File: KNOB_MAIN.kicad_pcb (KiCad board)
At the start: 2 copper layers, 100 x 30 mm, 25 parts, among them J1 HRO_TYPE-C-31-M-12, SW1 PEC11R-4220F-S0024, U1 LP2992AIM5X-3.3, U2 ESP32-C3-MINI-1

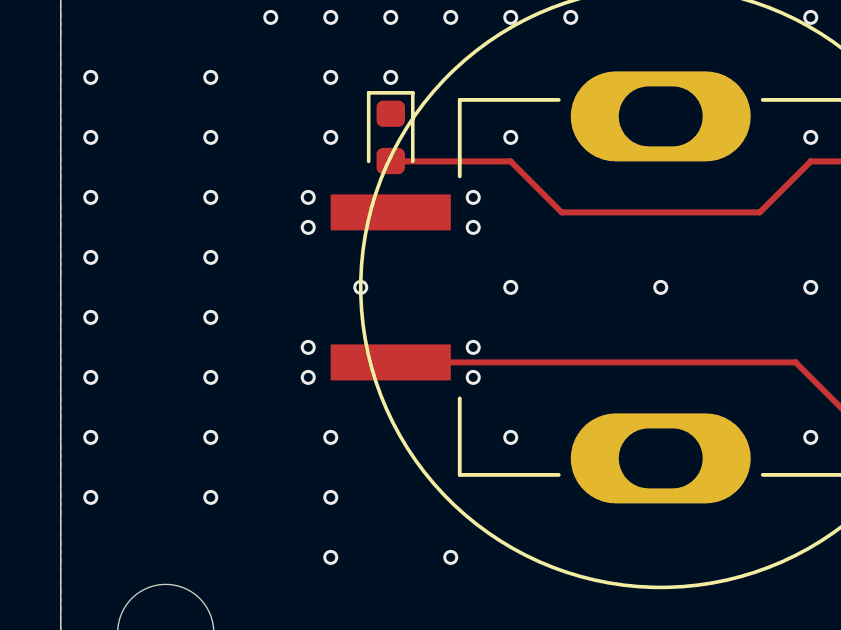
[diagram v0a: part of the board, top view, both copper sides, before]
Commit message: Add 100nF debounce capacitor to push pin
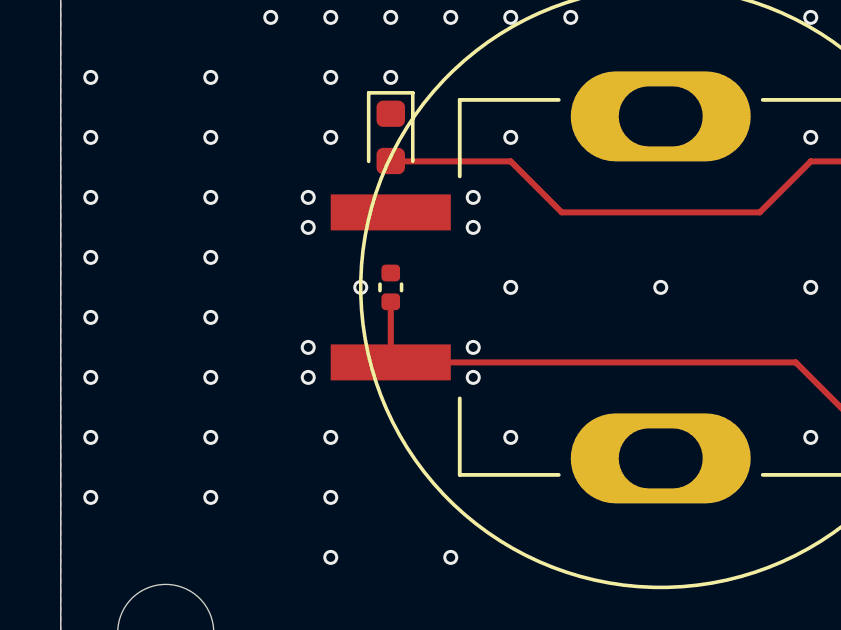
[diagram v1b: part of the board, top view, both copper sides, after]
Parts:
- added C7: 100nF, Capacitor_SMD:C_0402_1005Metric, F.Cu at (111.0, 85.0)
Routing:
- net /ENTER: track 76.2 -> 78.2 mm
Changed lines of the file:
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@@
     (thickness 1.6)
     (drawings 46)
-    (tracks 371)
+    (tracks 372)
     (zones 0)
-    (modules 25)
+    (modules 26)
     (nets 18)
   )
@@
     (diff_pair_width 0.28)
     (diff_pair_gap 0.15)
+  )
+  (module Capacitor_SMD:C_0402_1005Metric (layer F.Cu)
+    (at 111 85 90)
+    (descr "Capacitor SMD 0402 (1005 Metric), square (rectangular) end terminal, IPC_7351 nominal, (Body size source: IPC-SM-782 page 76, https://www.pcb-3d.com/wordpress/wp-content/uploads/ipc-sm-782a_amendment_1_and_2.pdf), generated with kicad-footprint-generator")
+    (tags capacitor)
+    (attr smd)
+    (fp_text reference C7 (at 0 -1.16 90) (layer F.Fab)
+      (effects (font (size 1 1) (thickness 0.15)))
+    )
+    (fp_text value 100nF (at 0 1.16 90) (layer F.Fab)
+      (effects (font (size 1 1) (thickness 0.15)))
+    )
+    (fp_line (start 0.91 0.46) (end -0.91 0.46) (layer F.CrtYd) (width 0.05))
+    (fp_line (start 0.91 -0.46) (end 0.91 0.46) (layer F.CrtYd) (width 0.05))
+    (fp_line (start -0.91 -0.46) (end 0.91 -0.46) (layer F.CrtYd) (width 0.05))
+    (fp_line (start -0.91 0.46) (end -0.91 -0.46) (layer F.CrtYd) (width 0.05))
+    (fp_line (start -0.107836 0.36) (end 0.107836 0.36) (layer F.SilkS) (width 0.12))
+    (fp_line (start -0.107836 -0.36) (end 0.107836 -0.36) (layer F.SilkS) (width 0.12))
+    (fp_line (start 0.5 0.25) (end -0.5 0.25) (layer F.Fab) (width 0.1))
+    (fp_line (start 0.5 -0.25) (end 0.5 0.25) (layer F.Fab) (width 0.1))
+    (fp_line (start -0.5 -0.25) (end 0.5 -0.25) (layer F.Fab) (width 0.1))
+    (fp_line (start -0.5 0.25) (end -0.5 -0.25) (layer F.Fab) (width 0.1))
+    (fp_text user %R (at 0 0 90) (layer F.Fab)
+      (effects (font (size 0.25 0.25) (thickness 0.04)))
+    )
+    (pad 2 smd roundrect (at 0.48 0 90) (size 0.56 0.62) (layers F.Cu F.Paste F.Mask) (roundrect_rratio 0.25)
+      (net 2 GND))
+    (pad 1 smd roundrect (at -0.48 0 90) (size 0.56 0.62) (layers F.Cu F.Paste F.Mask) (roundrect_rratio 0.25)
+      (net 9 /ENTER))
+    (model ${KISYS3DMOD}/Capacitor_SMD.3dshapes/C_0402_1005Metric.wrl
+      (at (xyz 0 0 0))
+      (scale (xyz 1 1 1))
+      (rotate (xyz 0 0 0))
+    )
   )
   (module Resistor_SMD:R_0402_1005Metric (layer F.Cu)
@@
   (segment (start 124.5 87.5) (end 134.5 97.5) (width 0.2) (layer F.Cu) (net 9))
   (segment (start 111 87.5) (end 124.5 87.5) (width 0.2) (layer F.Cu) (net 9))
+  (segment (start 111 85.48) (end 111 87.5) (width 0.2) (layer F.Cu) (net 9))
   (segment (start 125 80.8) (end 123.3 82.5) (width 0.2) (layer F.Cu) (net 10))
   (segment (start 123.3 82.5) (end 116.7 82.5) (width 0.2) (layer F.Cu) (net 10))
